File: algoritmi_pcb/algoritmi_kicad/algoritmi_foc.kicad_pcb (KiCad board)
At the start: 2 copper layers, 42 x 29.2 mm, 33 parts, among them IC2 AP2114HA-3.3TRG1, J2 53261-0371, J3 SMM-110-02-H-D-K-TR, U1 TMC6300-LA-T

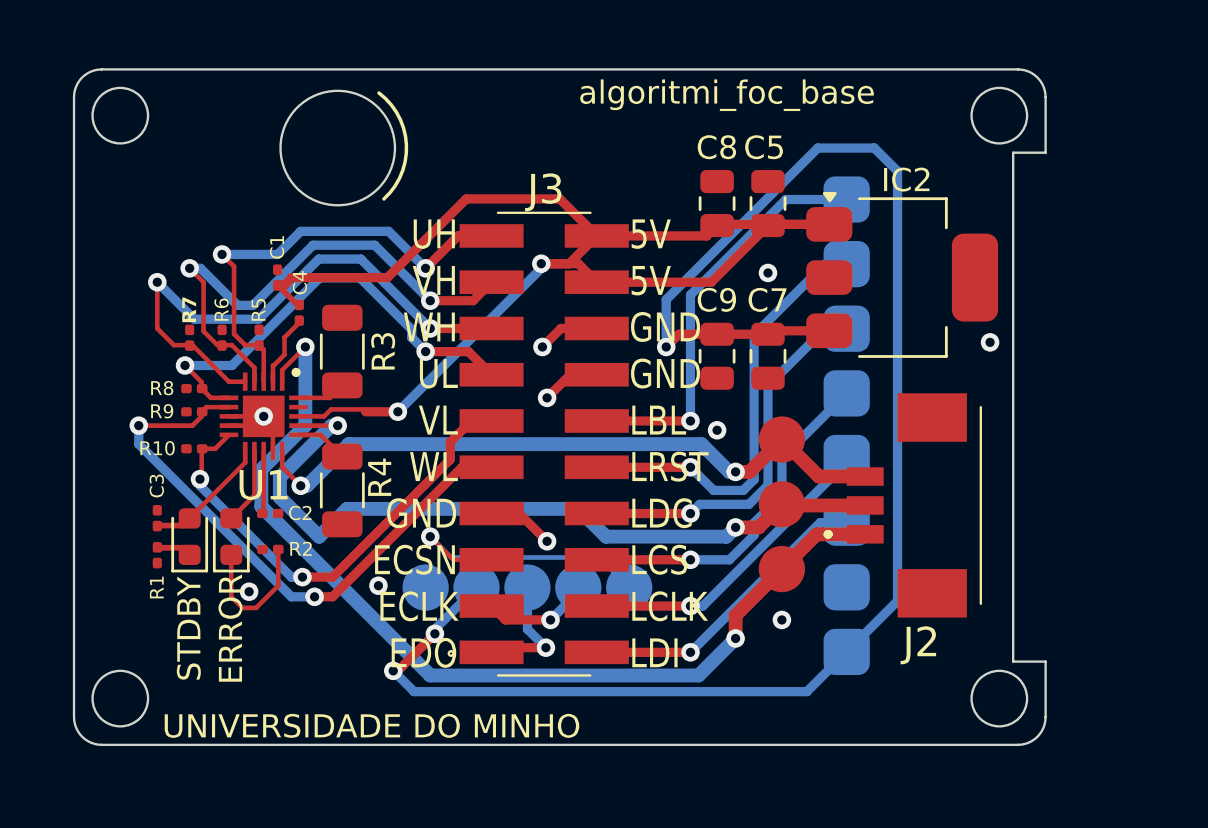
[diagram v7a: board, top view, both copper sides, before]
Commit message: Changed the base pcb and started motor pcb
The motor pcb is almost finished, just needs to get the encoder centered in the middle.
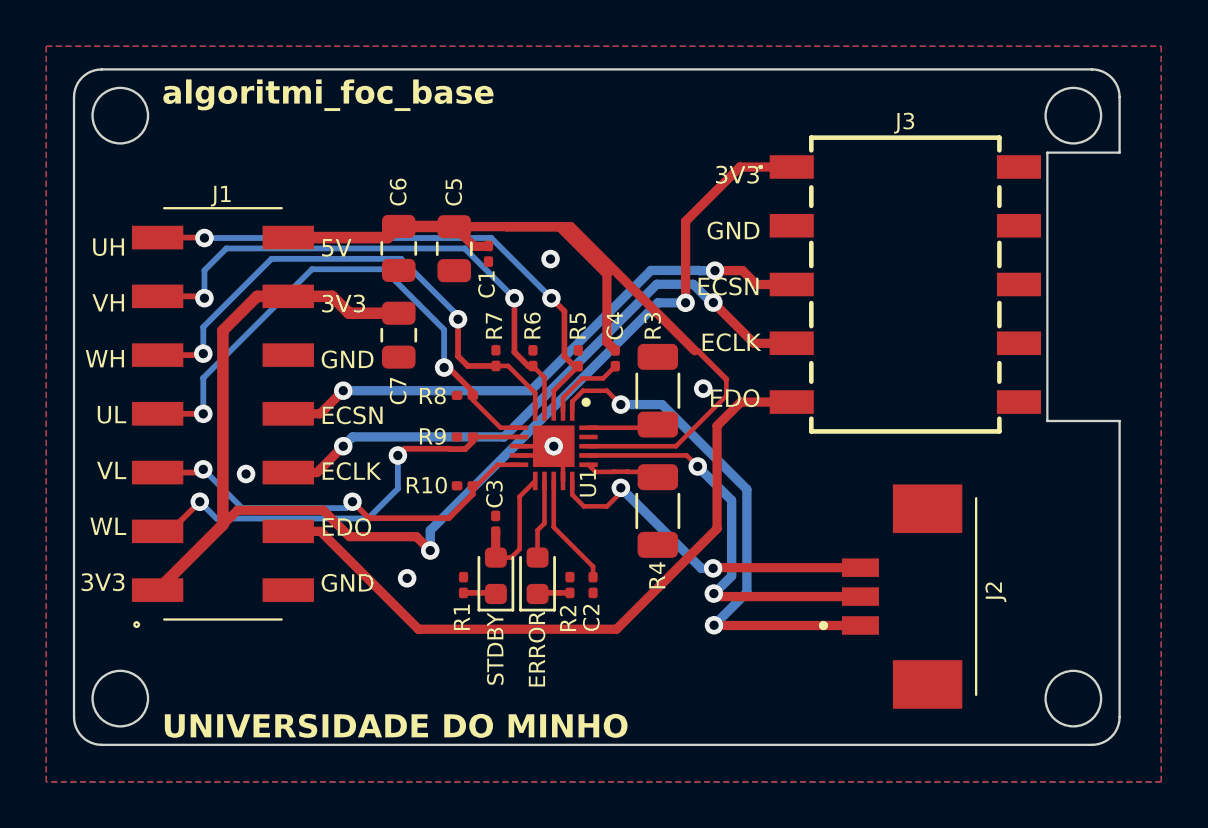
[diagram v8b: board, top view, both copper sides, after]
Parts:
- removed C8: 4.7uF 25V, Capacitor_SMD:C_0805_2012Metric
- removed C9: 10uF 25V, Capacitor_SMD:C_0805_2012Metric
- removed D1: STDBY, LED_SMD:LED_0603_1608Metric
- removed D2: ERROR, LED_SMD:LED_0603_1608Metric
- removed IC2: AP2114HA-3.3TRG1, Package_TO_SOT_SMD:SOT-223-3_TabPin2
- removed REF** (x8): SolderWirePad_1x01_SMD_1x2mm, Connector_Wire:SolderWirePad_1x01_SMD_1x2mm
- added C6: 4.7uF 25V, Capacitor_SMD:C_0805_2012Metric, F.Cu at (94.2, 74.7)
- added ERROR: ERROR, LED_SMD:LED_0603_1608Metric, F.Cu at (100.2, 88.9)
- added STDBY: STDBY, LED_SMD:LED_0603_1608Metric, F.Cu at (98.4, 88.9)
- J1: value ~ -> SSM-107-L-DV-P-TR; footprint solder_pads:solder_pads_2mm_8 -> SamacSys_Parts:SSM-107-XXX-DV-P-TR; moved to F.Cu
- J3: value SMM-110-02-H-D-K-TR -> SSM-105-L-SH; footprint SamacSys_Parts:SMM-110-02-XX-D-K-TR -> SamacSys_Parts:SSM105LSH
- moved J1 24.4 mm to (86.6, 81.9), turned to -90 degrees
- moved J3 17.1 mm to (116.1, 76.3)
- moved C7 16.0 mm to (94.2, 78.5)
- moved C3 14.6 mm to (98.4, 86.6)
- moved C2 14.3 mm to (102.6, 89.3), turned to 90 degrees
- moved R5 13.8 mm to (102.0, 79.5)
- moved C4 13.8 mm to (103.6, 79.5)
- moved R3 13.7 mm to (105.4, 80.9)
- moved C5 13.7 mm to (96.6, 74.8), turned to 90 degrees
- moved R4 13.7 mm to (105.4, 86.1)
- moved R6 13.5 mm to (100.0, 79.5)
- moved R1 13.3 mm to (97.0, 89.3), turned to -90 degrees
- moved R7 13.3 mm to (98.4, 79.5)
- moved R2 13.0 mm to (101.6, 89.3), turned to -90 degrees
- moved U1 12.6 mm to (100.9, 83.3)
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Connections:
- C1 pad 2: VS -> +5V
- C4 pad 1: VS -> +5V
- C5 pad 2: VS -> +5V
- J1 pad 3: LCD_DATA_IN -> WL
- J1 pad 4: LCD_CLOCK -> E_DO
- J1 pad 5: LCD_CS -> VL
- J1 pad 6: LCD_DC -> E_CLK
- J1 pad 7: LCD_RESET -> UL
- J1 pad 8: LCD_BL -> E_CSN
- U1 pad 18: VS -> +5V
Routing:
- net VS: track 57.7 -> 0.00 mm, vias 2 -> 0
- net +5V: track 0.00 -> 39.9 mm
- net E_DO: track 5.36 -> 30.2 mm, vias 1 -> 0
- net E_CLK: track 4.70 -> 26.2 mm, vias 1 -> 2
- net W_OUT: track 41.8 -> 22.7 mm
- net LCD_RESET: track 18.9 -> 0.00 mm, vias 1 -> 0
- net LCD_BL: track 18.0 -> 0.00 mm, vias 1 -> 0
- net LCD_DC: track 16.6 -> 0.00 mm, vias 1 -> 0
- net V_OUT: track 33.6 -> 17.7 mm
- net LCD_CS: track 15.0 -> 0.00 mm, vias 1 -> 0
- net LCD_CLOCK: track 13.6 -> 0.00 mm, vias 1 -> 0
- net U_OUT: track 28.7 -> 15.2 mm
- net LCD_DATA_IN: track 13.1 -> 0.00 mm, vias 1 -> 0
- net E_CSN: track 12.6 -> 24.6 mm, vias 1 -> 2
- net +3.3V: track 70.1 -> 59.9 mm, vias 3 -> 2
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- added copper zone on B.Cu, net GND
- added copper zone on F.Cu, net GND
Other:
- board size 42 x 29.2 mm -> 45.2 x 29.2 mm
- board text added: "3V3 GND ECSN ECLK EDO"
- board text added: "5V 3V3 GND ECSN ECLK EDO GND"
- board text added: "UH VH WH UL VL WL 3V3"
- board text removed: "5V 5V GND GND LBL LRST LDC LCS LCLK LDI"
- board text removed: "BL RST DC CS CLK DI GND 3.3V"
- board text removed: "ENC"
- board text removed: "GND 3.3V DO CLK CSN"
- board text removed: "UH VH WH UL VL WL GND ECSN ECLK EDO"
